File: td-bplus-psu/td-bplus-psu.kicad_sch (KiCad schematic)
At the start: 24 parts, among them J1 Conn_01x08_Pin, U14 LT3758AEMSE

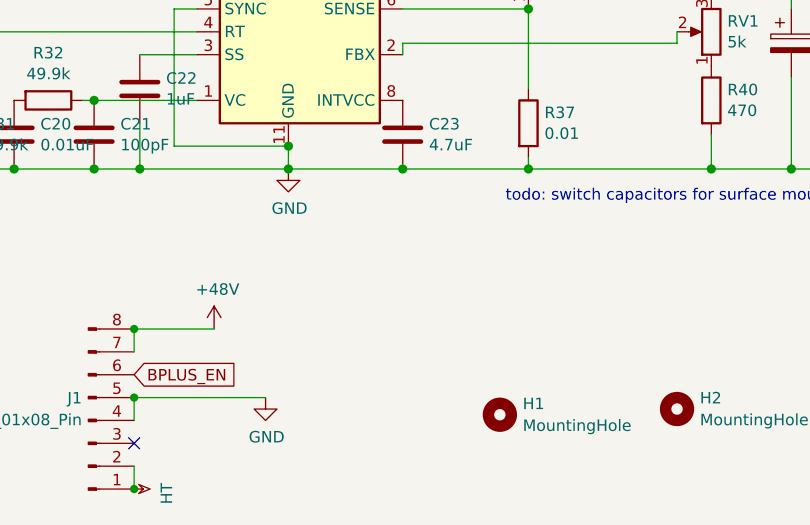
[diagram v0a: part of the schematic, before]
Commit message: Add note to fix on td-bplus-psu
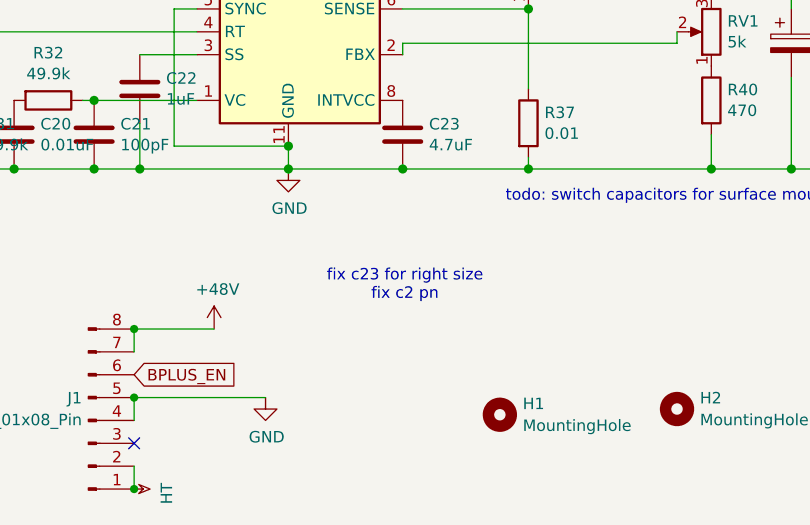
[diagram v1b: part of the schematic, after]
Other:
- note added: "fix c23 for right size fix c2 pn"
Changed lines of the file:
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@@
 	(generator_version "9.0")
 	(paper "A4")
+	(text "fix c23 for right size\nfix c2 pn"
+		(exclude_from_sim no)
+		(at 90.424 72.644 0)
+		(effects
+			(font
+				(size 1.27 1.27)
+			)
+		)
+	)
 	(text "todo: switch capacitors for surface mount"
 		(exclude_from_sim no)
